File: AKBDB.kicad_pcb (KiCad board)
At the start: 2 copper layers, 32.8 x 8.1 mm, 9 parts, among them J1 TYPE-C-31-M12_13, J2 SM04B-SRSS-TB(LF)(SN), U1 USBLC6-2SC6

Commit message: small fixes
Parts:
- R1, R2: footprint Resistor_SMD:R_0603_1608Metric -> Resistor_SMD:R_0402_1005Metric
- moved R2 0.60 mm to (41.1, 61.6)
- moved J2 0.50 mm to (33.1, 63.2)
- moved R1 0.45 mm to (53.8, 60.6)
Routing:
- net VCC: track 14.1 -> 13.0 mm, vias 0 -> 2
- net GND: track 4.42 -> 5.07 mm
- net DP: track 7.00 -> 6.45 mm
- net GNDPWR: track 22.5 -> 23.1 mm, vias 4 -> 2
- net VBUS: track 17.5 -> 17.0 mm

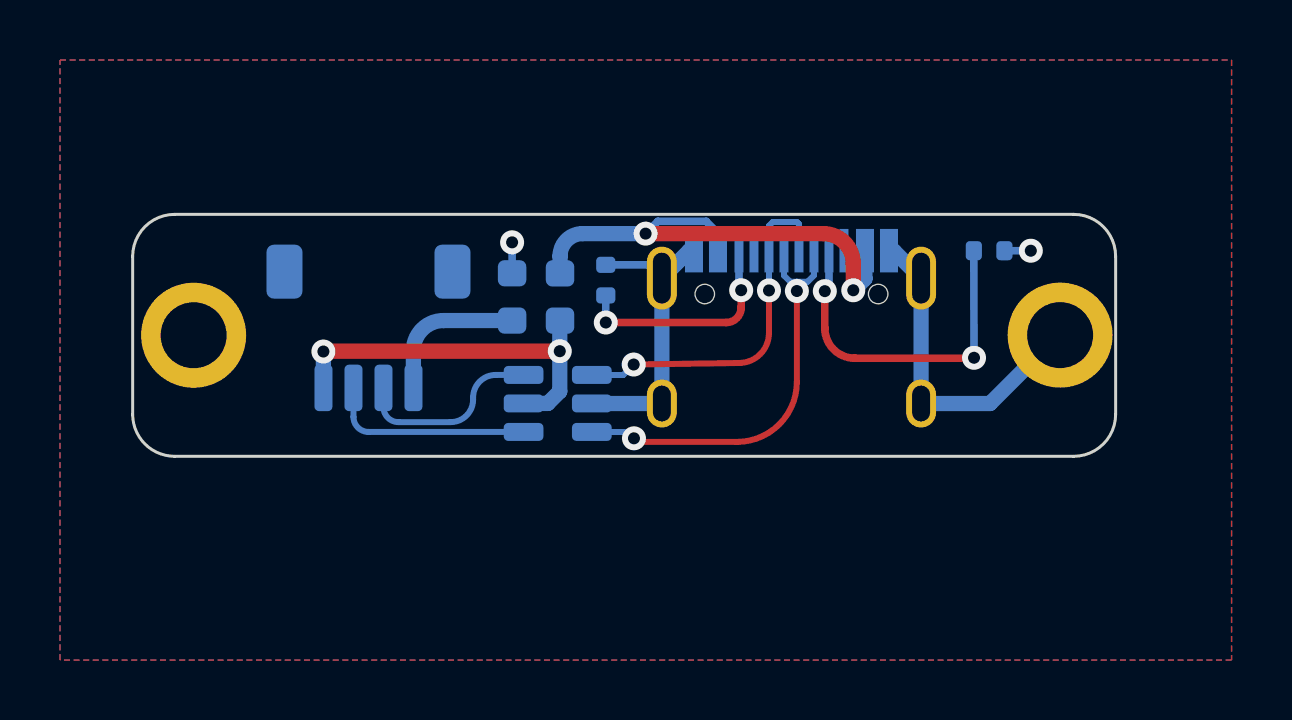
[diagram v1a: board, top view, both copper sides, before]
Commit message: slight adjustments to the datalines
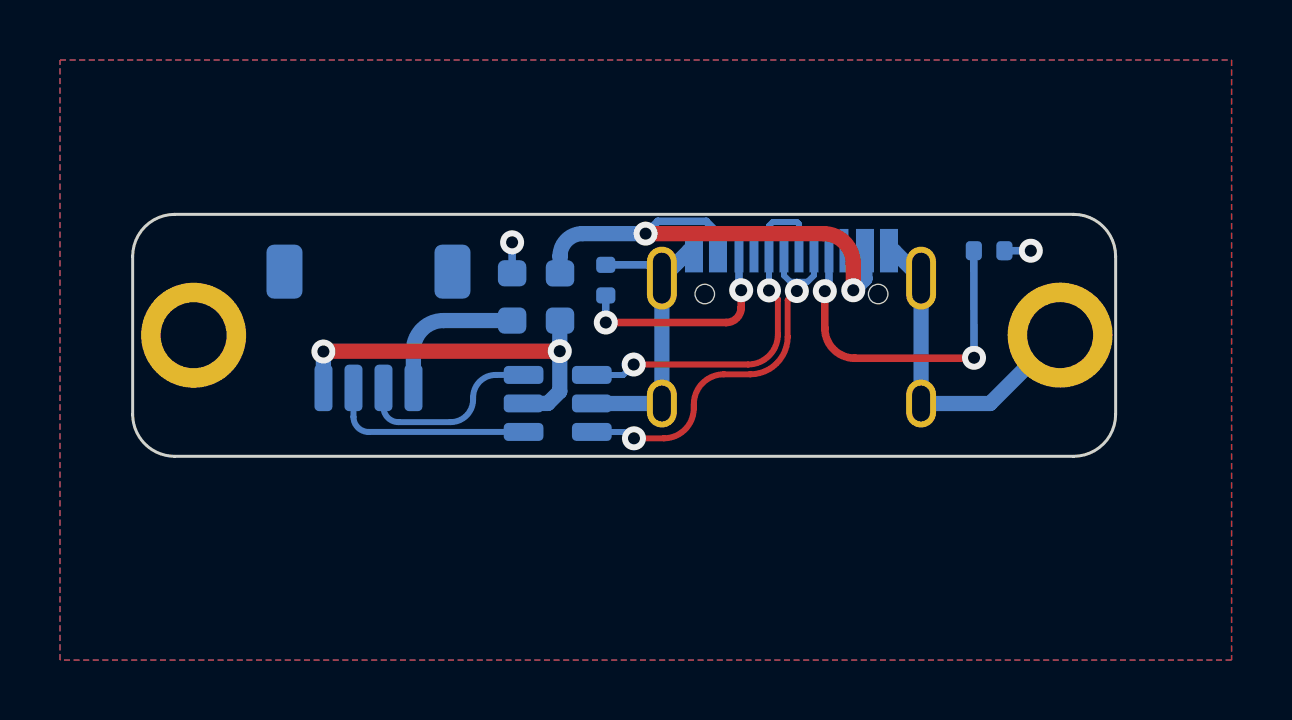
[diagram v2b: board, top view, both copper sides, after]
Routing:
- net DBus-: track 14.2 -> 13.3 mm
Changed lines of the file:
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@@
   (via (at 31.64 64.01) (size 0.8) (drill 0.4) (layers "F.Cu" "B.Cu") (net 2))
   (segment (start 31.64 64.01) (end 31.64 65.4205) (width 0.508) (layer "B.Cu") (net 2))
-  (segment (start 31.64 65.4205) (end 31.6425 65.423) (width 0.508) (layer "B.Cu") (net 2))
   (segment (start 39.12 65.74) (end 38.3125 65.74) (width 0.508) (layer "B.Cu") (net 2))
   (segment (start 39.51908 62.98892) (end 39.51908 65.34092) (width 0.508) (layer "B.Cu") (net 2))
@@
   (segment (start 49.6925 61.584022) (end 49.6925 60.648) (width 0.508) (layer "B.Cu") (net 5))
   (arc (start 39.5275 60.83) (mid 39.74717 60.29967) (end 40.2775 60.08) (width 0.508) (layer "B.Cu") (net 5))
-  (segment (start 46.4925 63.392309) (end 46.4925 61.973) (width 0.2) (layer "F.Cu") (net 8))
-  (segment (start 41.9825 64.443) (end 45.506911 64.392205) (width 0.2) (layer "F.Cu") (net 8))
+  (segment (start 46.79 62.2705) (end 46.79 63.443) (width 0.2) (layer "F.Cu") (net 8))
+  (segment (start 46.4925 61.973) (end 46.79 62.2705) (width 0.2) (layer "F.Cu") (net 8))
+  (segment (start 41.9825 64.443) (end 45.79 64.443) (width 0.2) (layer "F.Cu") (net 8))
   (via (at 46.4925 61.973) (size 0.8) (drill 0.4) (layers "F.Cu" "B.Cu") (net 8))
   (via (at 41.9825 64.443) (size 0.8) (drill 0.4) (layers "F.Cu" "B.Cu") (net 8))
-  (arc (start 45.506911 64.392205) (mid 46.204684 64.094302) (end 46.4925 63.392309) (width 0.2) (layer "F.Cu") (net 8))
+  (arc (start 46.79 63.443) (mid 46.497107 64.150107) (end 45.79 64.443) (width 0.2) (layer "F.Cu") (net 8))
   (segment (start 47.4925 59.763) (end 47.4925 60.648) (width 0.2) (layer "B.Cu") (net 8))
   (segment (start 46.4925 60.648) (end 46.4925 61.973) (width 0.2) (layer "B.Cu") (net 8))
@@
   (segment (start 47.4225 59.693) (end 47.4925 59.763) (width 0.2) (layer "B.Cu") (net 8))
   (segment (start 46.4925 59.819978) (end 46.619478 59.693) (width 0.2) (layer "B.Cu") (net 8))
-  (segment (start 42.1125 67.023) (end 45.4225 67.023) (width 0.2) (layer "F.Cu") (net 9))
-  (segment (start 47.4225 61.993) (end 47.4225 65.023) (width 0.2) (layer "F.Cu") (net 9))
-  (segment (start 41.9925 66.903) (end 42.1125 67.023) (width 0.2) (layer "F.Cu") (net 9))
+  (segment (start 43.987 65.903) (end 43.987 65.76952) (width 0.2) (layer "F.Cu") (net 9))
+  (segment (start 47.11652 62.29348) (end 47.11652 63.51952) (width 0.2) (layer "F.Cu") (net 9))
+  (segment (start 47.4225 61.993) (end 47.417 61.993) (width 0.2) (layer "F.Cu") (net 9))
+  (segment (start 41.9925 66.903) (end 42.987 66.903) (width 0.2) (layer "F.Cu") (net 9))
+  (segment (start 47.417 61.993) (end 47.11652 62.29348) (width 0.2) (layer "F.Cu") (net 9))
+  (segment (start 45.86652 64.76952) (end 44.987 64.76952) (width 0.2) (layer "F.Cu") (net 9))
   (via (at 47.4225 61.993) (size 0.8) (drill 0.4) (layers "F.Cu" "B.Cu") (net 9))
   (via (at 41.9925 66.903) (size 0.8) (drill 0.4) (layers "F.Cu" "B.Cu") (net 9))
-  (arc (start 47.4225 65.023) (mid 46.836714 66.437214) (end 45.4225 67.023) (width 0.2) (layer "F.Cu") (net 9))
+  (arc (start 42.987 66.903) (mid 43.694107 66.610107) (end 43.987 65.903) (width 0.2) (layer "F.Cu") (net 9))
+  (arc (start 43.987 65.76952) (mid 44.279893 65.062413) (end 44.987 64.76952) (width 0.2) (layer "F.Cu") (net 9))
+  (arc (start 47.11652 63.51952) (mid 46.750403 64.403403) (end 45.86652 64.76952) (width 0.2) (layer "F.Cu") (net 9))
   (segment (start 47.7825 61.683) (end 47.4225 61.683) (width 0.2) (layer "B.Cu") (net 9))
   (segment (start 41.7825 66.693) (end 41.9925 66.903) (width 0.2) (layer "B.Cu") (net 9))
